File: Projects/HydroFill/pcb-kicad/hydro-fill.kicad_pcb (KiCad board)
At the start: 2 copper layers, 108.8 x 78.4 mm, 31 parts, among them J1 12V 5A, J2 Solenoid output, J3 Pressure transmitter, J4 Temperature, J5 Display TFT 1.77'', J6 Status LEDs, J7 Manual Start Btn, Q1 S8050, Q2 S8050, Q3 IRFZ44N, Q4 S8050

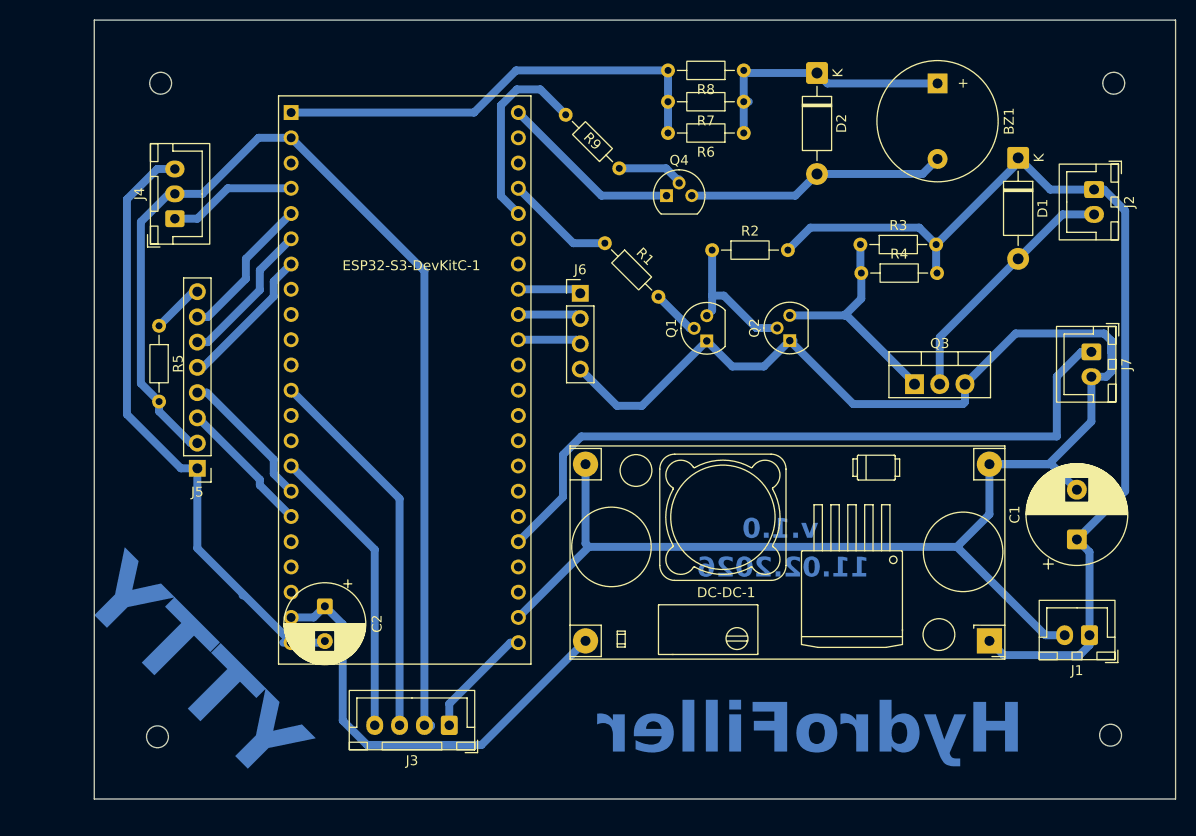
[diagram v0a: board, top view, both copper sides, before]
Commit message: [HydroFiller][PCB] Add `ESP Power Of When USB connected` connector
- Remove 1000mF capacitor
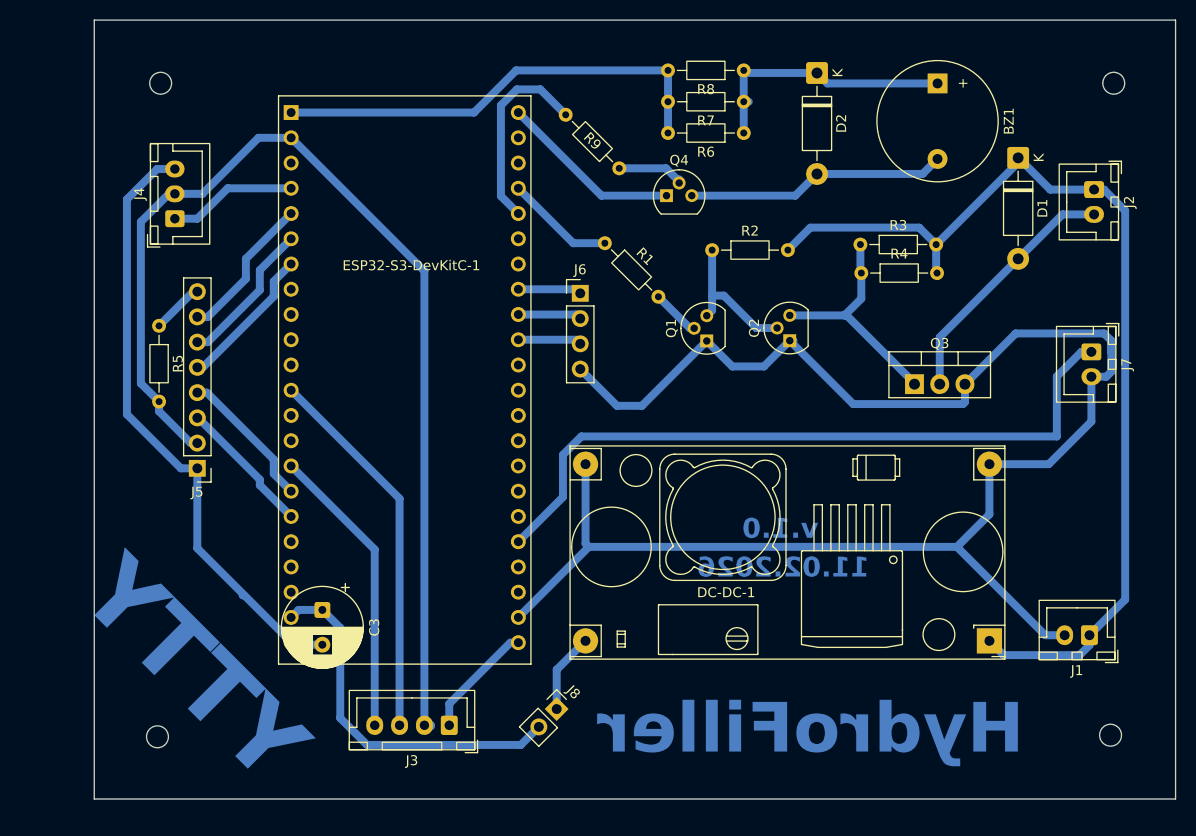
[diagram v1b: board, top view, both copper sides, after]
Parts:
- removed C1: 1000uF 25V, Capacitor_THT:CP_Radial_D10.0mm_P5.00mm
- removed C2: 470uF 16V, Capacitor_THT:CP_Radial_D8.0mm_P3.50mm
- added C3: 470uF 16V, Capacitor_THT:CP_Radial_D8.0mm_P3.50mm, F.Cu at (109.2, 117.9)
- added J8: ESP Power Off When USB, Connector_PinHeader_2.54mm:PinHeader_1x02_P2.54mm_Vertical, F.Cu at (132.8, 127.9)
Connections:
- ESP32-S3-DevKitC-1 pad 21: Net-(DC-DC-1-Vout) -> Net-(ESP32-S3-DevKitC-1-5Vin)
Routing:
- net Net-(DC-DC-1-Vout): track 45.9 -> 8.06 mm
- net Net-(ESP32-S3-DevKitC-1-5Vin): track 0.00 -> 36.9 mm
- net GND: track 273.2 -> 261.1 mm
- net +12V: track 101.9 -> 100.9 mm

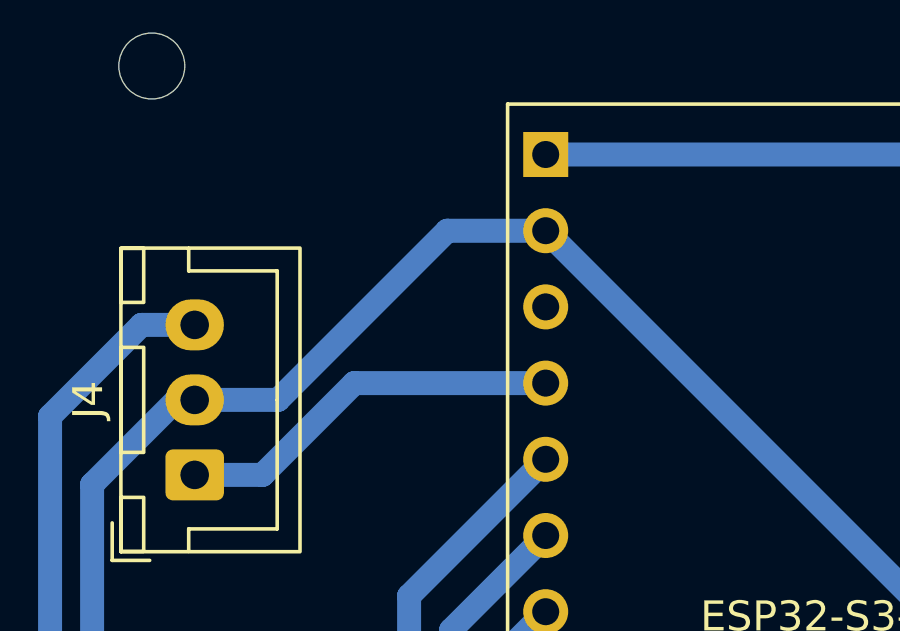
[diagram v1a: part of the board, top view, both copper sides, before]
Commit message: [HydroFiller][PCB] Add resistor 4.7kOm to out of temperature sensor
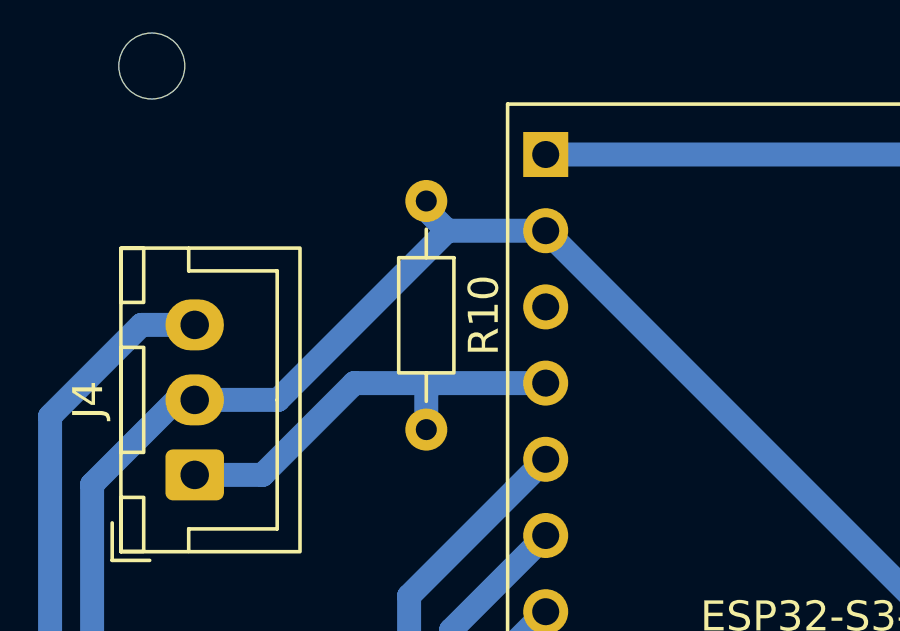
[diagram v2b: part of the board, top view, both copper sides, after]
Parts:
- added R10: 4,7k, Resistor_THT:R_Axial_DIN0204_L3.6mm_D1.6mm_P7.62mm_Horizontal, F.Cu at (102.1, 69.4)
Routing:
- net Net-(J4-Pin_1): track 13.0 -> 14.6 mm
- net Net-(J3-Pin_2): track 155.0 -> 156.3 mm
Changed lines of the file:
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@@
 		)
 	)
+	(footprint "Resistor_THT:R_Axial_DIN0204_L3.6mm_D1.6mm_P7.62mm_Horizontal"
+		(layer "F.Cu")
+		(at 102.07 69.4 -90)
+		(descr "Resistor, Axial_DIN0204 series, Axial, Horizontal, pin pitch=7.62mm, 0.167W, length*diameter=3.6*1.6mm^2, http://cdn-reichelt.de/documents/datenblatt/B400/1_4W%23YAG.pdf")
+		(tags "Resistor Axial_DIN0204 series Axial Horizontal pin pitch 7.62mm 0.167W length 3.6mm diameter 1.6mm")
+		(property "Reference" "R10"
+			(at 3.81 -1.92 90)
+			(layer "F.SilkS")
+			(effects
+				(font
+					(size 1 1)
+					(thickness 0.15)
+				)
+			)
+		)
+		(property "Value" "4,7k"
+			(at 3.81 1.92 90)
+			(layer "F.Fab")
+			(effects
+				(font
+					(size 1 1)
+					(thickness 0.15)
+				)
+			)
+		)
+		(property "Datasheet" "~"
+			(at 0 0 90)
+			(layer "F.Fab")
+			(hide yes)
+			(effects
+				(font
+					(size 1.27 1.27)
+					(thickness 0.15)
+				)
+			)
+		)
+		(property "Description" "Resistor"
+			(at 0 0 90)
+			(layer "F.Fab")
+			(hide yes)
+			(effects
+				(font
+					(size 1.27 1.27)
+					(thickness 0.15)
+				)
+			)
+		)
+		(property ki_fp_filters "R_*")
+		(sheetname "/")
+		(sheetfile "hydro-fill.kicad_sch")
+		(attr through_hole)
+		(fp_line
+			(start 0.94 0)
+			(end 1.89 0)
+			(stroke
+				(width 0.12)
+				(type solid)
+			)
+			(layer "F.SilkS")
+		)
+		(fp_line
+			(start 6.68 0)
+			(end 5.73 0)
+			(stroke
+				(width 0.12)
+				(type solid)
+			)
+			(layer "F.SilkS")
+		)
+		(fp_rect
+			(start 1.89 -0.92)
+			(end 5.73 0.92)
+			(stroke
+				(width 0.12)
+				(type solid)
+			)
+			(fill no)
+			(layer "F.SilkS")
+		)
+		(fp_rect
+			(start -0.95 -1.05)
+			(end 8.57 1.05)
+			(stroke
+				(width 0.05)
+				(type solid)
+			)
+			(fill no)
+			(layer "F.CrtYd")
+		)
+		(fp_line
+			(start 0 0)
+			(end 2.01 0)
+			(stroke
+				(width 0.1)
+				(type solid)
+			)
+			(layer "F.Fab")
+		)
+		(fp_line
+			(start 7.62 0)
+			(end 5.61 0)
+			(stroke
+				(width 0.1)
+				(type solid)
+			)
+			(layer "F.Fab")
+		)
+		(fp_rect
+			(start 2.01 -0.8)
+			(end 5.61 0.8)
+			(stroke
+				(width 0.1)
+				(type solid)
+			)
+			(fill no)
+			(layer "F.Fab")
+		)
+		(fp_text user "${REFERENCE}"
+			(at 3.81 0 90)
+			(layer "F.Fab")
+			(effects
+				(font
+					(size 0.72 0.72)
+					(thickness 0.108)
+				)
+			)
+		)
+		(pad "1" thru_hole circle
+			(at 0 0 270)
+			(size 1.4 1.4)
+			(drill 0.7)
+			(layers "*.Cu" "*.Mask")
+			(remove_unused_layers no)
+			(net 27 "Net-(J3-Pin_2)")
+			(pintype "passive")
+		)
+		(pad "2" thru_hole circle
+			(at 7.62 0 270)
+			(size 1.4 1.4)
+			(drill 0.7)
+			(layers "*.Cu" "*.Mask")
+			(remove_unused_layers no)
+			(net 26 "Net-(J4-Pin_1)")
+			(pintype "passive")
+		)
+		(embedded_fonts no)
+		(model "${KICAD9_3DMODEL_DIR}/Resistor_THT.3dshapes/R_Axial_DIN0204_L3.6mm_D1.6mm_P7.62mm_Horizontal.step"
+			(offset
+				(xyz 0 0 0)
+			)
+			(scale
+				(xyz 1 1 1)
+			)
+			(rotate
+				(xyz 0 0 0)
+			)
+		)
+	)
 	(footprint "Connector_JST:JST_XH_B2B-XH-A_1x02_P2.50mm_Vertical"
 		(layer "F.Cu")
@@
 	)
 	(segment
-		(start 99.67 75.47)
+		(start 102.2 75.47)
 		(end 106.05 75.47)
 		(width 0.8)
@@
 	)
 	(segment
+		(start 102.07 75.6)
+		(end 102.2 75.47)
+		(width 0.8)
+		(layer "B.Cu")
+		(net 26)
+	)
+	(segment
 		(start 94.35 78.53)
 		(end 96.61 78.53)
@@
 	)
 	(segment
+		(start 99.67 75.47)
+		(end 102.2 75.47)
+		(width 0.8)
+		(layer "B.Cu")
+		(net 26)
+	)
+	(segment
+		(start 102.07 77.02)
+		(end 102.07 75.6)
+		(width 0.8)
+		(layer "B.Cu")
+		(net 26)
+	)
+	(segment
 		(start 143.97 69.91)
 		(end 143.97 66.76)
@@
 	)
 	(segment
+		(start 102.07 69.691314)
+		(end 102.768686 70.39)
+		(width 0.8)
+		(layer "B.Cu")
+		(net 27)
+	)
+	(segment
 		(start 92.76 96.93)
 		(end 92.76 97.919949)
 		(width 0.8)
 		(layer "B.Cu")
+		(net 27)
+	)
+	(segment
+		(start 102.07 69.4)
+		(end 102.07 69.691314)
+		(width 0.8)
+		(layer "B.Cu")
